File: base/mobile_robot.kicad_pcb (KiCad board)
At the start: 2 copper layers, 85.6 x 49 mm, 74 parts, among them J1 USB_B_Micro, J2 Conn_02x05_Odd_Even, J3 Motor Power, J4 Conn_01x06, J5 Conn_01x06, Q1 BSS138, Q2 BSS138, Q3 BSS138, Q4 BSS138, SW1 SW_SPDT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

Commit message: Pretty much finished pcb layout and routing
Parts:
- added H1: MountingHole, MountingHole:MountingHole_3.2mm_M3, F.Cu at (25.4, 28.3)
- added H2: MountingHole, MountingHole:MountingHole_3.2mm_M3, F.Cu at (82.5, 28.3)
- added H3: MountingHole, MountingHole:MountingHole_3.2mm_M3, F.Cu at (25.4, 69.8)
- added H4: MountingHole, MountingHole:MountingHole_3.2mm_M3, F.Cu at (82.5, 69.8)
- SW1: footprint Button_Switch_THT:SW_E-Switch_EG1224_SPDT_Angled -> Button_Switch_SMD:SW_SPDT_PCM12
- moved R23 35.0 mm to (31.8, 61.8), turned to 0 degrees
- moved R17 32.4 mm to (46.9, 33.1)
- moved Q3 32.0 mm to (32.4, 59.2), turned to -90 degrees
- moved R21 31.4 mm to (35.4, 32.6), turned to 180 degrees
- moved R25 30.8 mm to (36.6, 61.8), turned to 180 degrees
- moved R22 30.2 mm to (32.3, 56.5), turned to 180 degrees
- moved Q4 29.8 mm to (36.0, 59.2), turned to -90 degrees
- moved Q2 29.3 mm to (34.9, 35.3), turned to 90 degrees
- moved R19 28.8 mm to (38.1, 32.6), turned to 0 degrees
- moved R24 28.4 mm to (36.1, 56.5), turned to 180 degrees
- moved R20 26.9 mm to (34.8, 38.0), turned to 0 degrees
- moved J3 26.6 mm to (75.9, 49.0), turned to -90 degrees
- moved U6 26.6 mm to (47.0, 36.6)
- moved C21 26.5 mm to (42.7, 37.9)
- moved R13 26.4 mm to (46.9, 26.3)
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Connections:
- U2 pad 3: HSE_IN -> unconnected-(U2-Pad3)
- U2 pad 4: HSE_OUT -> unconnected-(U2-Pad4)
- U2 pad 5: unconnected-(U2-Pad5) -> HSE_IN
- U2 pad 6: unconnected-(U2-Pad6) -> HSE_OUT
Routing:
- net V_ENC: track 0.00 -> 122.9 mm, vias 0 -> 3
- net +12V: track 0.00 -> 75.0 mm
- net +3V3: track 0.00 -> 73.4 mm, vias 0 -> 17
- net GND: track 0.00 -> 69.1 mm, vias 0 -> 60
- net NRST: track 0.00 -> 47.1 mm, vias 0 -> 2
- net MB_IN2: track 0.00 -> 42.0 mm, vias 0 -> 2
- net MB_IN1: track 0.00 -> 39.9 mm, vias 0 -> 2
- net MB_RS: track 0.00 -> 35.5 mm, vias 0 -> 1
- net MA_OUT2: track 0.00 -> 33.4 mm
- net /MA_ENC_CH2_RAW: track 0.00 -> 32.8 mm, vias 0 -> 1
- net MB_EN: track 0.00 -> 32.8 mm, vias 0 -> 2
- net MA_EN: track 0.00 -> 32.0 mm, vias 0 -> 2
- net /MA_ENC_CH1_RAW: track 0.00 -> 30.9 mm, vias 0 -> 1
- net MA_OUT1: track 0.00 -> 30.7 mm, vias 0 -> 2
- net MA_IN2: track 0.00 -> 28.9 mm, vias 0 -> 2
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- added copper zone on F.Cu, net +3V3
- added copper zone on In2.Cu, net +3V3
- added copper zone on F.Cu, net GND
- added copper zone on In1.Cu, net GND
- added copper zone on In2.Cu, net GND
- added copper zone on F.Cu, net V_ENC
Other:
- board size 85.6 x 49 mm -> 65.3 x 49.7 mm
- copper layers 2 -> 4

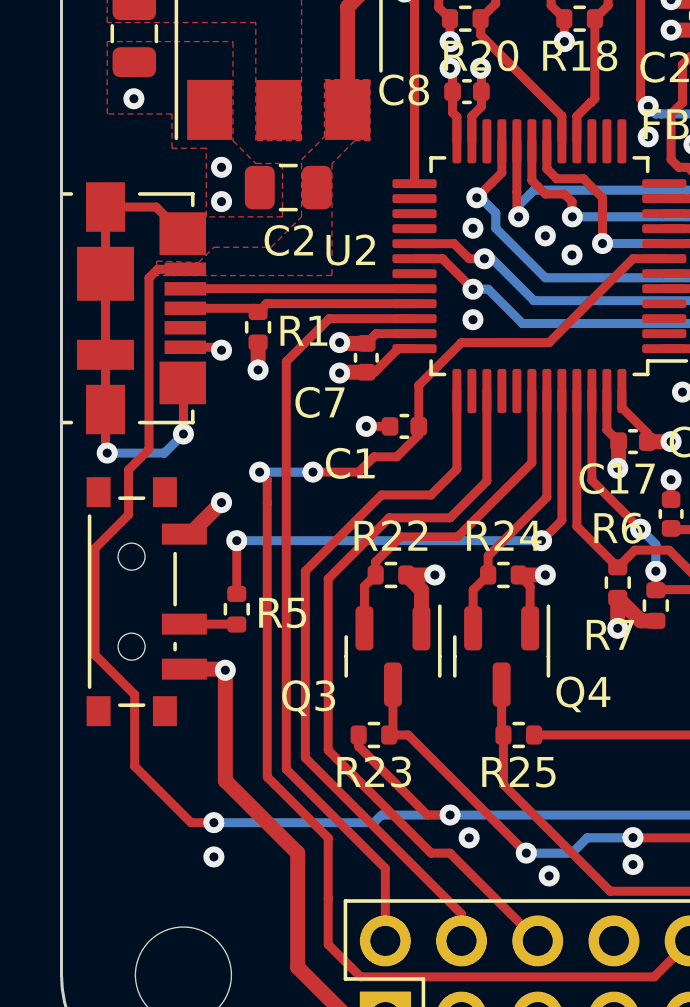
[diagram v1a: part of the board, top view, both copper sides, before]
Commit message: Did usb differential pair properly
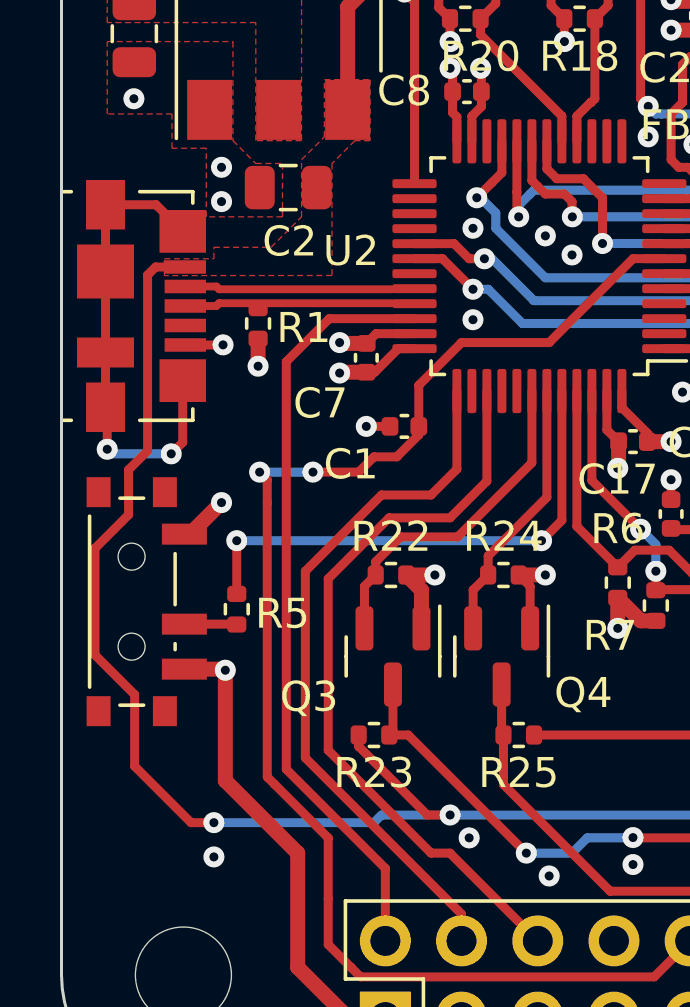
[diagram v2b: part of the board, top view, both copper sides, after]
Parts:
- moved R1 0.13 mm to (27.9, 48.1)
- moved J1 0.08 mm to (24.0, 47.5)
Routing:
- net USB_D+: track 7.81 -> 6.93 mm
- net USB_D-: track 7.64 -> 6.93 mm

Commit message: Finished PCB
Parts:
- moved U4 9.25 mm to (57.6, 55.9)
- moved J5 6.35 mm to (54.0, 71.4), turned to 180 degrees
- moved J4 6.35 mm to (69.0, 27.8), turned to 180 degrees
- moved J2 5.24 mm to (37.2, 70.0), turned to 0 degrees
- moved J3 2.92 mm to (73.0, 49.1), turned to 180 degrees
- moved C19 2.04 mm to (66.4, 50.6), turned to -90 degrees
- moved U6 0.30 mm to (47.3, 36.6), turned to 90 degrees
- moved Q3 0.15 mm to (32.3, 59.1), turned to 90 degrees
- moved U3 0.13 mm to (45.0, 55.9), turned to 0 degrees
- moved U5 0.13 mm to (47.0, 29.6), turned to 90 degrees
- turned U1 to -90 degrees
- turned Q1 to -90 degrees
- turned Q2 to -90 degrees
- turned Q4 to 90 degrees
- turned U2 to 90 degrees
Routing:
- net +12V: track 75.0 -> 79.5 mm
- net GND: track 69.1 -> 69.3 mm, vias 60 -> 59
